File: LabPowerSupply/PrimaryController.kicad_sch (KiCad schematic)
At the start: 25 parts, among them Y1 8M

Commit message: almost done
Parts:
- C10_Power1, C1_Power1, C2_Power1, C3_Power1, C4_Power1, C5_Power1, C6_Power1, C7_Power1, C8_Power1, C9_Power1: footprint Capacitor_SMD:C_0805_2012Metric -> Capacitor_SMD:C_0603_1608Metric
- gave numbers to parts that had none: 1
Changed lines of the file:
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@@
     (property "Reference" "C4_Power1" (id 0) (at 132.08 15.24 90))
     (property "Value" "1u" (id 1) (at 132.08 17.78 90))
-    (property "Footprint" "Capacitor_SMD:C_0805_2012Metric" (id 2) (at 135.89 21.8948 0)
+    (property "Footprint" "Capacitor_SMD:C_0603_1608Metric" (id 2) (at 135.89 21.8948 0)
       (effects (font (size 1.27 1.27)) hide)
     )
@@
     (property "Reference" "C8_Power1" (id 0) (at 120.65 31.75 90))
     (property "Value" "100n" (id 1) (at 120.65 34.29 90))
-    (property "Footprint" "Capacitor_SMD:C_0805_2012Metric" (id 2) (at 124.46 26.9748 0)
+    (property "Footprint" "Capacitor_SMD:C_0603_1608Metric" (id 2) (at 124.46 26.9748 0)
       (effects (font (size 1.27 1.27)) hide)
     )
@@
     (property "Reference" "C5_Power1" (id 0) (at 143.51 15.24 90))
     (property "Value" "1u" (id 1) (at 143.51 17.78 90))
-    (property "Footprint" "Capacitor_SMD:C_0805_2012Metric" (id 2) (at 147.32 21.8948 0)
+    (property "Footprint" "Capacitor_SMD:C_0603_1608Metric" (id 2) (at 147.32 21.8948 0)
       (effects (font (size 1.27 1.27)) hide)
     )
@@
   (symbol (lib_id "Connector_Generic:Conn_02x08_Counter_Clockwise") (at 72.39 156.21 0) (unit 1)
     (in_bom yes) (on_board yes) (fields_autoplaced)
-    (property "Reference" "Front_Panel?" (id 0) (at 73.66 142.24 0))
+    (property "Reference" "Front_Panel1" (id 0) (at 73.66 142.24 0))
     (property "Value" "Conn_02x10_Counter_Clockwise" (id 1) (at 73.66 144.78 0))
     (property "Footprint" "Connector_IDC:IDC-Header_2x10_P2.54mm_Vertical" (id 2) (at 72.39 156.21 0)
@@
     (property "Reference" "C9_Power1" (id 0) (at 132.08 31.75 90))
     (property "Value" "100n" (id 1) (at 132.08 34.29 90))
-    (property "Footprint" "Capacitor_SMD:C_0805_2012Metric" (id 2) (at 135.89 26.9748 0)
+    (property "Footprint" "Capacitor_SMD:C_0603_1608Metric" (id 2) (at 135.89 26.9748 0)
       (effects (font (size 1.27 1.27)) hide)
     )
@@
     (property "Reference" "C2_Power1" (id 0) (at 109.22 15.24 90))
     (property "Value" "1u" (id 1) (at 109.22 17.78 90))
-    (property "Footprint" "Capacitor_SMD:C_0805_2012Metric" (id 2) (at 113.03 21.8948 0)
+    (property "Footprint" "Capacitor_SMD:C_0603_1608Metric" (id 2) (at 113.03 21.8948 0)
       (effects (font (size 1.27 1.27)) hide)
     )
@@
     (property "Reference" "C1_Power1" (id 0) (at 97.79 15.24 90))
     (property "Value" "1u" (id 1) (at 97.79 17.78 90))
-    (property "Footprint" "Capacitor_SMD:C_0805_2012Metric" (id 2) (at 101.6 21.8948 0)
+    (property "Footprint" "Capacitor_SMD:C_0603_1608Metric" (id 2) (at 101.6 21.8948 0)
       (effects (font (size 1.27 1.27)) hide)
     )
@@
     (property "Reference" "C6_Power1" (id 0) (at 97.79 31.75 90))
     (property "Value" "100n" (id 1) (at 97.79 34.29 90))
-    (property "Footprint" "Capacitor_SMD:C_0805_2012Metric" (id 2) (at 101.6 26.9748 0)
+    (property "Footprint" "Capacitor_SMD:C_0603_1608Metric" (id 2) (at 101.6 26.9748 0)
       (effects (font (size 1.27 1.27)) hide)
     )
@@
     (property "Reference" "C7_Power1" (id 0) (at 109.22 31.75 90))
     (property "Value" "100n" (id 1) (at 109.22 34.29 90))
-    (property "Footprint" "Capacitor_SMD:C_0805_2012Metric" (id 2) (at 113.03 26.9748 0)
+    (property "Footprint" "Capacitor_SMD:C_0603_1608Metric" (id 2) (at 113.03 26.9748 0)
       (effects (font (size 1.27 1.27)) hide)
     )
@@
     (property "Reference" "C10_Power1" (id 0) (at 143.51 31.75 90))
     (property "Value" "100n" (id 1) (at 143.51 34.29 90))
-    (property "Footprint" "Capacitor_SMD:C_0805_2012Metric" (id 2) (at 147.32 26.9748 0)
+    (property "Footprint" "Capacitor_SMD:C_0603_1608Metric" (id 2) (at 147.32 26.9748 0)
       (effects (font (size 1.27 1.27)) hide)
     )
@@
     (property "Reference" "C3_Power1" (id 0) (at 120.65 15.24 90))
     (property "Value" "1u" (id 1) (at 120.65 17.78 90))
-    (property "Footprint" "Capacitor_SMD:C_0805_2012Metric" (id 2) (at 124.46 21.8948 0)
-      (effects (font (size 1.27 1.27)) hide)
-    )
+    (property "Footprint" "Capacitor_SMD:C_0603_1608Metric" (id 2) (at 124.46 21.8948 0)
+      (effects (font (size 1.27 1.27)) hide)
+    )

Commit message: SMD Oscillator
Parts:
- Y1: footprint Crystal:Crystal_HC18-U_Vertical -> Crystal:Crystal_SMD_HC49-SD
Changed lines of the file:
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@@
       (effects (font (size 1.27 1.27)) (justify right))
     )
-    (property "Footprint" "Crystal:Crystal_HC18-U_Vertical" (id 2) (at 93.98 78.74 0)
+    (property "Footprint" "Crystal:Crystal_SMD_HC49-SD" (id 2) (at 93.98 78.74 0)
       (effects (font (size 1.27 1.27)) hide)
     )

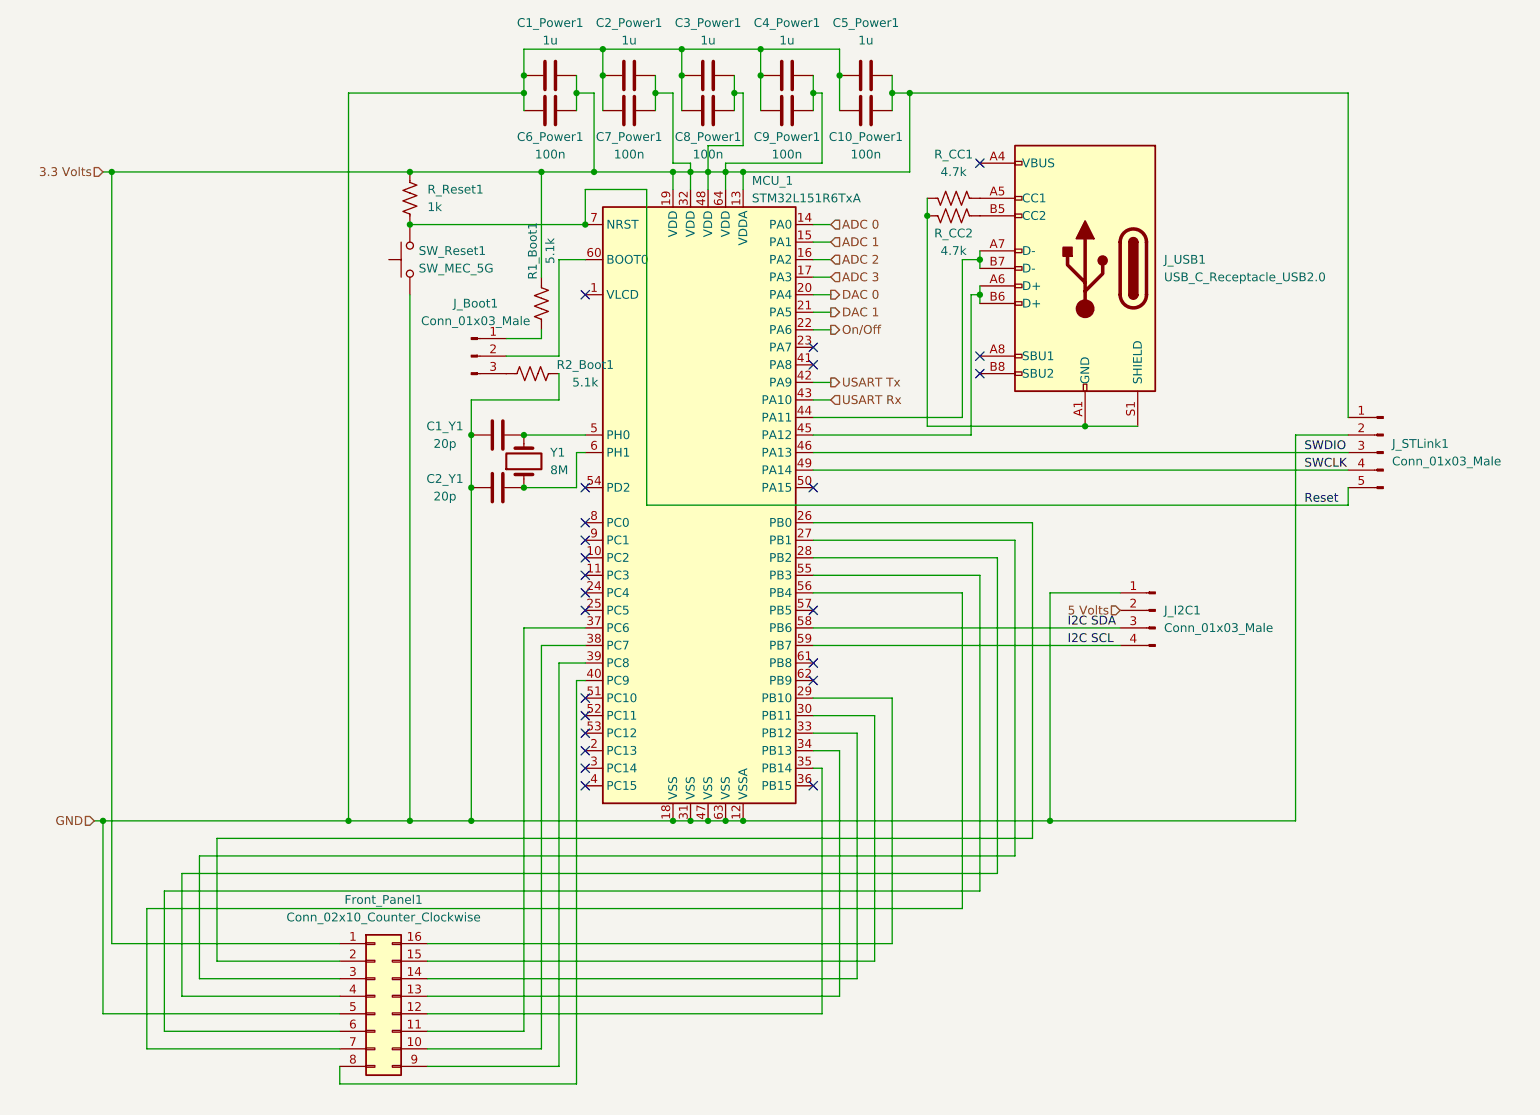
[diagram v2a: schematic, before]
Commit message: removed transformer and bug squached
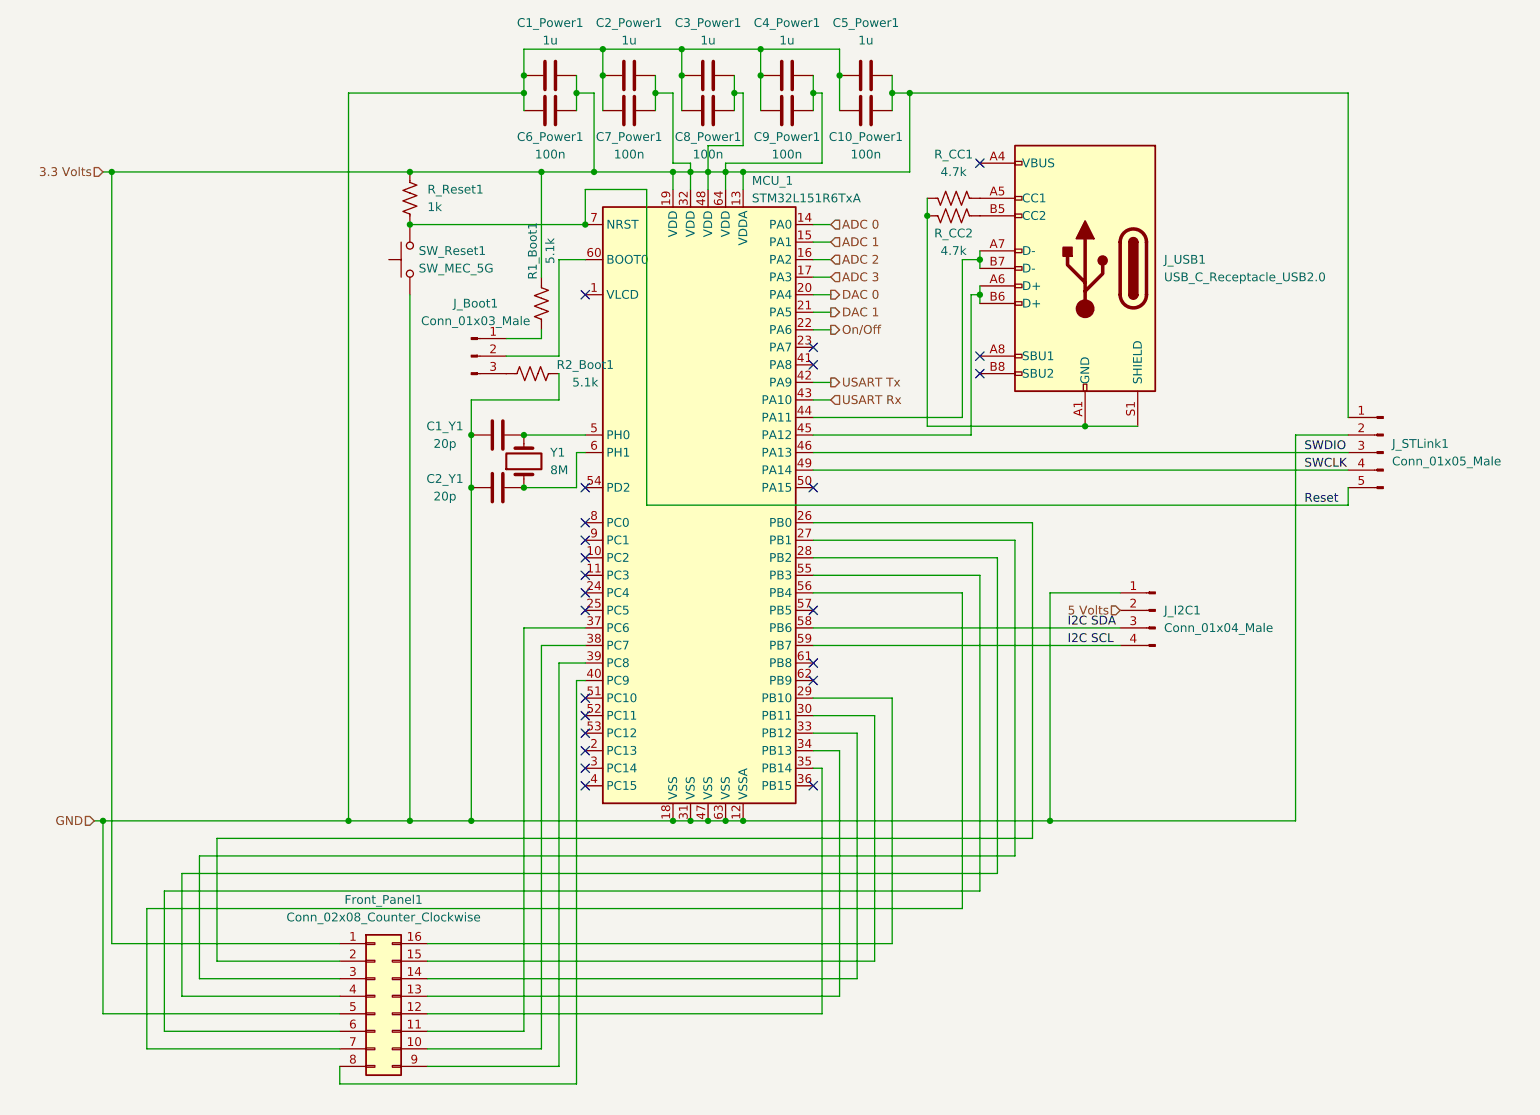
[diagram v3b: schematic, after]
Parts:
- Front_Panel1: value Conn_02x10_Counter_Clockwise -> Conn_02x08_Counter_Clockwise; footprint Connector_IDC:IDC-Header_2x10_P2.54mm_Vertical -> Connector_IDC:IDC-Header_2x08_P2.54mm_Vertical
- J_I2C1: value Conn_01x03_Male -> Conn_01x04_Male; footprint Connector_PinHeader_2.54mm:PinHeader_1x03_P2.54mm_Vertical -> Connector_PinHeader_2.54mm:PinHeader_1x04_P2.54mm_Vertical
- J_STLink1: value Conn_01x03_Male -> Conn_01x05_Male; footprint Connector_PinHeader_2.54mm:PinHeader_1x03_P2.54mm_Vertical -> Connector_PinHeader_2.54mm:PinHeader_1x05_P2.54mm_Vertical
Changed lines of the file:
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@@
       (effects (font (size 1.27 1.27)) (justify right))
     )
-    (property "Value" "Conn_01x03_Male" (id 1) (at 186.69 102.8699 0)
-      (effects (font (size 1.27 1.27)) (justify right))
-    )
-    (property "Footprint" "Connector_PinHeader_2.54mm:PinHeader_1x03_P2.54mm_Vertical" (id 2) (at 185.42 100.33 0)
+    (property "Value" "Conn_01x04_Male" (id 1) (at 186.69 102.8699 0)
+      (effects (font (size 1.27 1.27)) (justify right))
+    )
+    (property "Footprint" "Connector_PinHeader_2.54mm:PinHeader_1x04_P2.54mm_Vertical" (id 2) (at 185.42 100.33 0)
       (effects (font (size 1.27 1.27)) hide)
     )
@@
     (in_bom yes) (on_board yes) (fields_autoplaced)
     (property "Reference" "Front_Panel1" (id 0) (at 73.66 142.24 0))
-    (property "Value" "Conn_02x10_Counter_Clockwise" (id 1) (at 73.66 144.78 0))
-    (property "Footprint" "Connector_IDC:IDC-Header_2x10_P2.54mm_Vertical" (id 2) (at 72.39 156.21 0)
+    (property "Value" "Conn_02x08_Counter_Clockwise" (id 1) (at 73.66 144.78 0))
+    (property "Footprint" "Connector_IDC:IDC-Header_2x08_P2.54mm_Vertical" (id 2) (at 72.39 156.21 0)
       (effects (font (size 1.27 1.27)) hide)
     )
@@
       (effects (font (size 1.27 1.27)) (justify right))
     )
-    (property "Value" "Conn_01x03_Male" (id 1) (at 219.71 78.7399 0)
-      (effects (font (size 1.27 1.27)) (justify right))
-    )
-    (property "Footprint" "Connector_PinHeader_2.54mm:PinHeader_1x03_P2.54mm_Vertical" (id 2) (at 218.44 77.47 0)
-      (effects (font (size 1.27 1.27)) hide)
-    )
+    (property "Value" "Conn_01x05_Male" (id 1) (at 219.71 78.7399 0)
+      (effects (font (size 1.27 1.27)) (justify right))
+    )
+    (property "Footprint" "Connector_PinHeader_2.54mm:PinHeader_1x05_P2.54mm_Vertical" (id 2) (at 218.44 77.47 0)
+      (effects (font (size 1.27 1.27)) hide)
+    )

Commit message: routing is weird
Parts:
- SW_Reset1: footprint Button_Switch_SMD:SW_MEC_5GSH9 -> Button_Switch_THT:SW_PUSH-12mm
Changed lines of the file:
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@@
   (junction (at 116.84 19.05) (diameter 0) (color 0 0 0 0)
   )
+  (junction (at 77.47 44.45) (diameter 0) (color 0 0 0 0)
+  )
   (junction (at 128.27 19.05) (diameter 0) (color 0 0 0 0)
   )
@@
   )
   (junction (at 170.18 130.81) (diameter 0) (color 0 0 0 0)
-  )
-  (junction (at 77.47 44.45) (diameter 0) (color 0 0 0 0)
   )
   (junction (at 77.47 130.81) (diameter 0) (color 0 0 0 0)
@@
       (effects (font (size 1.27 1.27)) (justify right))
     )
-    (property "Footprint" "Button_Switch_SMD:SW_MEC_5GSH9" (id 2) (at 72.39 49.53 0)
-      (effects (font (size 1.27 1.27)) hide)
-    )
+    (property "Footprint" "Button_Switch_THT:SW_PUSH-12mm" (id 2) (at 72.39 49.53 0)
+      (effects (font (size 1.27 1.27)) hide)
+    )

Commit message: Traces
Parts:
- SW_Reset1: symbol Switch:SW_MEC_5G -> Switch:SW_Push
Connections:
- net GND: no longer SW_Reset1.2 (A)
- net Reset: now also SW_Reset1.2; no longer SW_Reset1.3 (B), SW_Reset1.4 (B)
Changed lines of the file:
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@@
     (pin "9")
   )
-  (symbol (lib_id "Switch:SW_MEC_5G") (at 77.47 49.53 90) (unit 1)
+  (symbol (lib_id "Switch:SW_Push") (at 77.47 49.53 90) (unit 1)
     (in_bom yes) (on_board yes) (fields_autoplaced)
     (property "Reference" "SW_Reset1" (id 0) (at 78.74 48.2599 90)
@@
       (effects (font (size 1.27 1.27)) hide)
     )
-    (property "Datasheet" "http://www.apem.com/int/index.php?controller=attachment&id_attachment=488" (id 3) (at 72.39 49.53 0)
+    (property "Datasheet" "~" (id 3) (at 72.39 49.53 0)
       (effects (font (size 1.27 1.27)) hide)
     )
     (pin "1")
-    (pin "3")
     (pin "2")
-    (pin "4")
   )
   (symbol (lib_id "Device:C") (at 132.08 27.94 90) (unit 1)
